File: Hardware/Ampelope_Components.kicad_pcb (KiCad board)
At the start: 4 copper layers, 60.5 x 81.6 mm, 101 parts, among them J1 Conn_01x12_Male, J18 SWD_Header, J19 USB_B_Micro, J2 Conn_01x12_Male, J3 Conn_01x12_Male, J4 Conn_01x12_Male, J5 Eurorack_16_pin_power, Q1 MMBT3906, Q2 MMBT3906, Q3 MMBT3906, Q4 MMBT3906, Q5 MMBT3906, U1 STM32G431RB, U2 AS3364, U3 LM1117-3.3, U4 TL074, U5 TL074, U6 TL074, Y1 8MHz 20pF

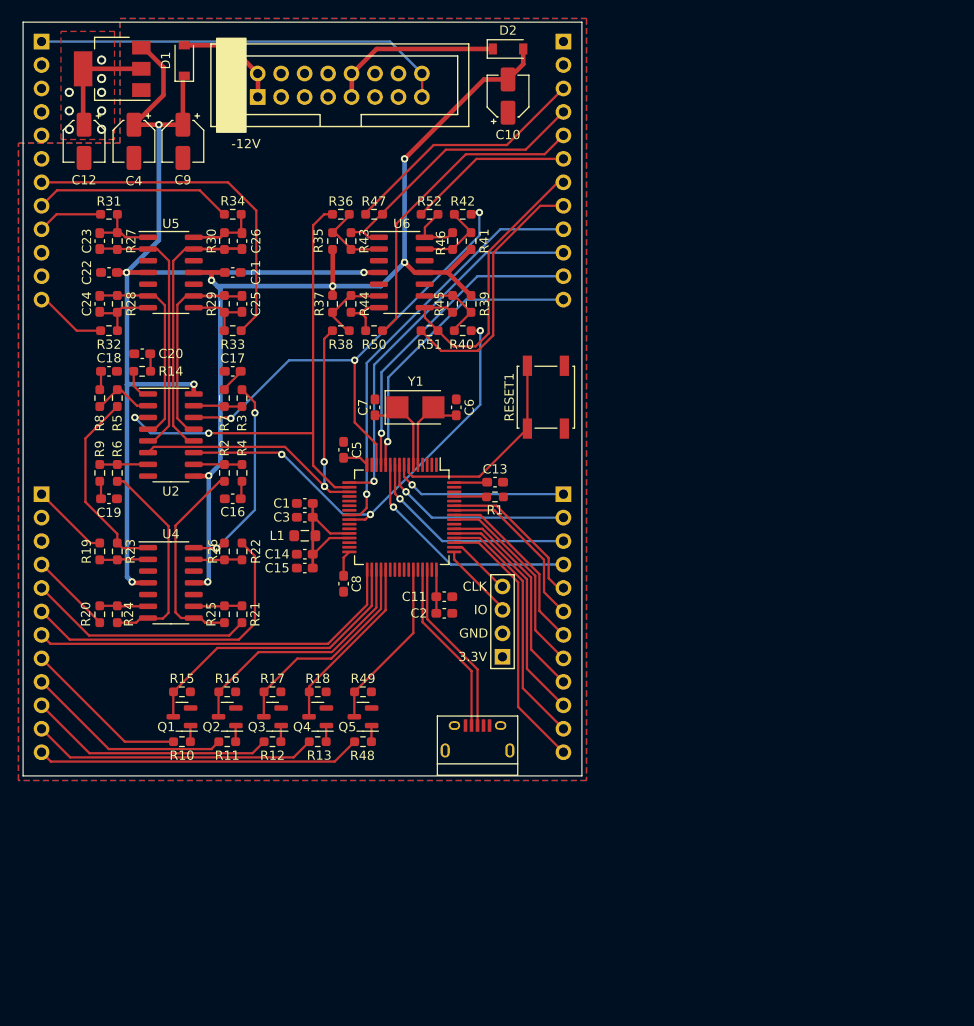
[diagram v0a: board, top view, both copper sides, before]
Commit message: Updates to component PCB to reflect VCA schematic changes
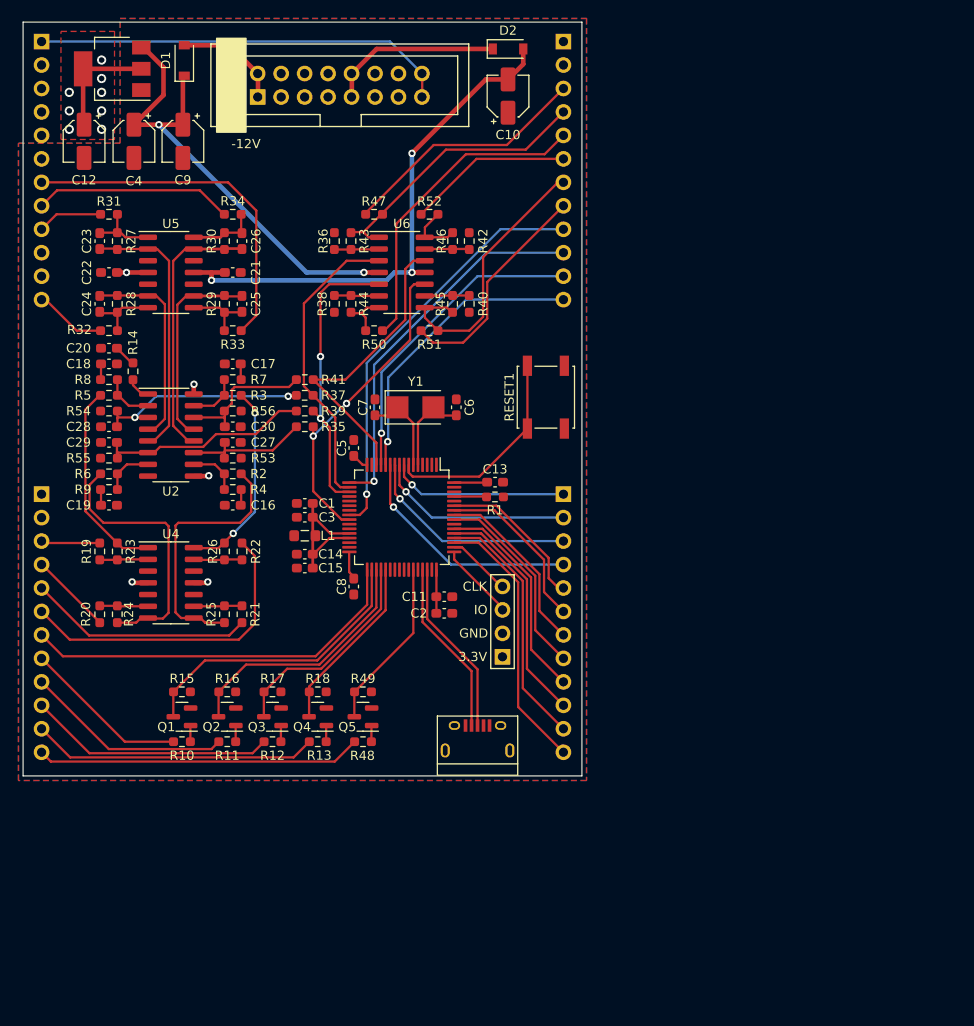
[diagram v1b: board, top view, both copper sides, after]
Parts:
- added C27: 2.2nF, Capacitor_SMD:C_0603_1608Metric_Pad1.08x0.95mm_HandSolder, F.Cu at (82.7, 70.9)
- added C28: 2.2nF, Capacitor_SMD:C_0603_1608Metric_Pad1.08x0.95mm_HandSolder, F.Cu at (69.3, 69.2)
- added C29: 2.2nF, Capacitor_SMD:C_0603_1608Metric_Pad1.08x0.95mm_HandSolder, F.Cu at (69.3, 70.9)
- added C30: 2.2nF, Capacitor_SMD:C_0603_1608Metric_Pad1.08x0.95mm_HandSolder, F.Cu at (82.7, 69.2)
- added R53: 10k, Resistor_SMD:R_0603_1608Metric_Pad0.98x0.95mm_HandSolder, F.Cu at (82.7, 72.6)
- added R54: 10k, Resistor_SMD:R_0603_1608Metric_Pad0.98x0.95mm_HandSolder, F.Cu at (69.3, 67.5)
- added R55: 10k, Resistor_SMD:R_0603_1608Metric_Pad0.98x0.95mm_HandSolder, F.Cu at (69.3, 72.6)
- added R56: 10k, Resistor_SMD:R_0603_1608Metric_Pad0.98x0.95mm_HandSolder, F.Cu at (82.7, 67.5)
- R35, R37, R39, R41: value 75k -> 6k8
- R36, R38, R40, R42: value 20k -> 3k3
- R43, R44, R45, R46: value 47k -> 4k7
- moved R41 23.4 mm to (90.5, 64.1), turned to 180 degrees
- moved R39 21.4 mm to (90.5, 67.5), turned to 180 degrees
- moved R35 20.3 mm to (90.5, 69.2), turned to 180 degrees
- moved R37 10.3 mm to (90.5, 65.8), turned to 180 degrees
- moved C20 3.65 mm to (69.3, 60.7)
- moved R36 2.98 mm to (93.7, 49.1), turned to 90 degrees
- moved R38 2.98 mm to (93.7, 55.9), turned to -90 degrees
- moved R40 2.98 mm to (108.3, 55.9), turned to -90 degrees
- moved R42 2.98 mm to (108.3, 49.1), turned to 90 degrees
- moved R8 2.24 mm to (69.3, 64.1), turned to 0 degrees
- moved R7 2.19 mm to (82.7, 64.1), turned to 180 degrees
- moved R4 2.06 mm to (82.7, 76.0), turned to 180 degrees
- moved R9 2.06 mm to (69.3, 76.0), turned to 0 degrees
- moved C8 1.14 mm to (95.8, 86.5)
- moved C5 1.12 mm to (95.8, 71.5)
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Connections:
- J19 pad 1: /USB_VBUS -> unconnected-(J19-Pad1)
- J2 pad 1: /Audio1_In -> unconnected-(J2-Pad1)
- J2 pad 3: unconnected-(J2-Pad3) -> /Audio1_In
- R35 pad 1: Net-(R35-Pad1) -> /Env3_DAC
- R35 pad 2: VEE -> /Env3_Scaled
- R36 pad 1: Net-(R35-Pad1) -> Net-(R36-Pad1)
- R36 pad 2: /Env1_DAC -> GND
- R37 pad 1: Net-(R37-Pad1) -> /Env1_DAC
- R37 pad 2: VEE -> /Env1_Scaled
- R38 pad 1: Net-(R37-Pad1) -> Net-(R38-Pad1)
- R38 pad 2: /Env2_DAC -> GND
- R39 pad 1: Net-(R39-Pad1) -> /Env2_DAC
- R39 pad 2: VEE -> /Env2_Scaled
- R40 pad 1: Net-(R39-Pad1) -> Net-(R40-Pad1)
- R40 pad 2: /Env3_DAC -> GND
- R41 pad 1: Net-(R41-Pad1) -> /Env4_DAC
- R41 pad 2: VEE -> /Env4_Scaled
- R42 pad 1: Net-(R41-Pad1) -> Net-(R42-Pad1)
- R42 pad 2: /Env4_DAC -> GND
- R43 pad 2: Net-(R35-Pad1) -> Net-(R36-Pad1)
- R44 pad 2: Net-(R37-Pad1) -> Net-(R38-Pad1)
- R45 pad 2: Net-(R39-Pad1) -> Net-(R40-Pad1)
- R46 pad 2: Net-(R41-Pad1) -> Net-(R42-Pad1)
- U2 pad 11: /Env3_DAC -> /Env3_Scaled
- U2 pad 14: /Env4_DAC -> /Env4_Scaled
- U2 pad 3: /Env1_DAC -> /Env1_Scaled
- U2 pad 6: /Env2_DAC -> /Env2_Scaled
- U6 pad 10: GND -> /Env3_DAC
- U6 pad 12: GND -> /Env4_DAC
- U6 pad 13: Net-(R41-Pad1) -> Net-(R42-Pad1)
- U6 pad 2: Net-(R35-Pad1) -> Net-(R36-Pad1)
- U6 pad 3: GND -> /Env1_DAC
- U6 pad 5: GND -> /Env2_DAC
- U6 pad 6: Net-(R37-Pad1) -> Net-(R38-Pad1)
- U6 pad 9: Net-(R39-Pad1) -> Net-(R40-Pad1)
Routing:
- net /Env1_Scaled: track 0.00 -> 23.5 mm, vias 0 -> 2
- net /Env1_DAC: track 55.0 -> 32.5 mm, vias 2 -> 0
- net /Env2_Scaled: track 0.00 -> 22.3 mm
- net /Env4_DAC: track 54.9 -> 32.7 mm, vias 3 -> 0
- net /Env3_DAC: track 50.2 -> 34.3 mm, vias 3 -> 2
- net /Env4_Scaled: track 0.00 -> 15.1 mm
- net VEE: track 110.0 -> 95.9 mm, vias 6 -> 5
- net /Env3_Scaled: track 0.00 -> 13.9 mm
- net /Env2_DAC: track 41.3 -> 31.5 mm
- net Net-(R39-Pad1): track 8.14 -> 0.00 mm
- net Net-(R41-Pad1): track 8.08 -> 0.00 mm
- net Net-(R37-Pad1): track 8.05 -> 0.00 mm
- net Net-(R35-Pad1): track 8.04 -> 0.00 mm
- net /Audio3_In_Buff: track 21.7 -> 27.8 mm
- net /Audio2_In_Buff: track 22.1 -> 28.2 mm
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
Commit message: Added test points to component PCB; Added 3D mockups
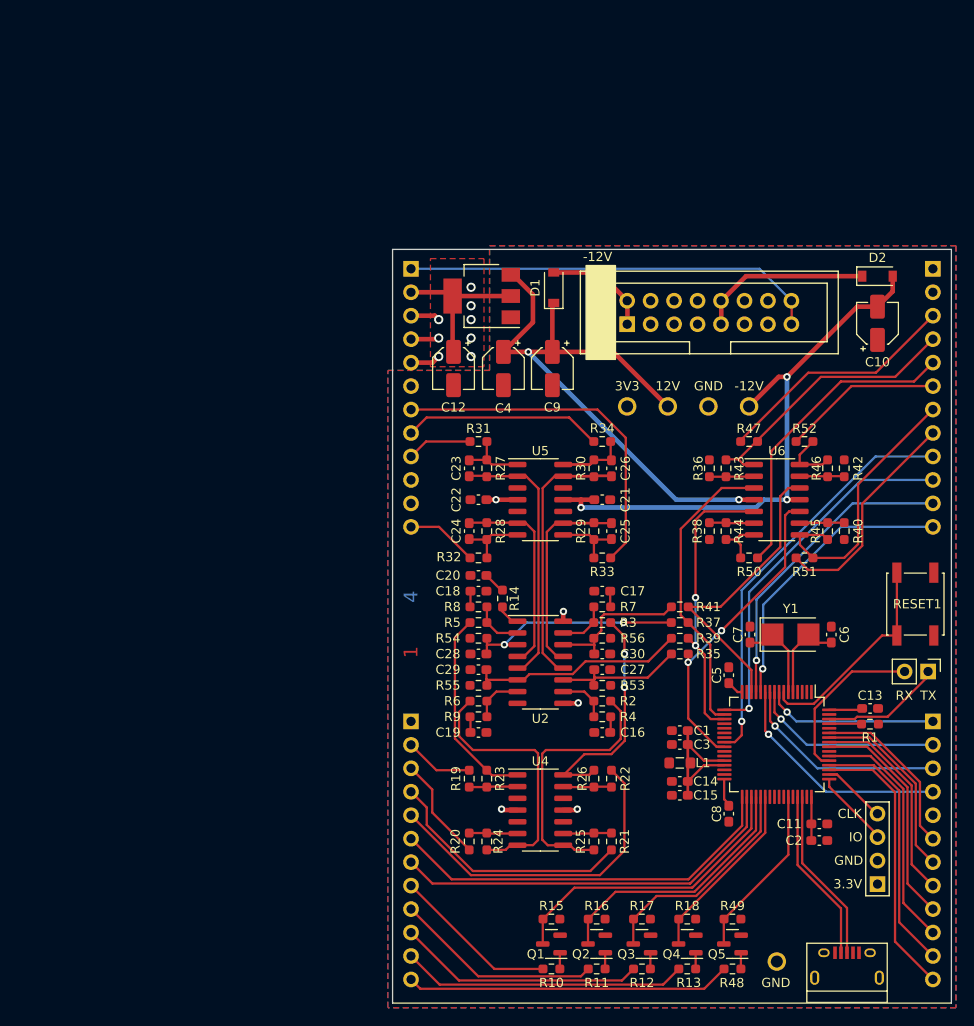
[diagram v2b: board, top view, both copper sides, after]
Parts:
- added FID1: 4_Layer_Marker, Custom_Footprints:4_Layer_Markers, F.Cu at (102.0, 90.6)
- added J6: Conn_01x02_Male, Connector_PinHeader_2.54mm:PinHeader_1x02_P2.54mm_Vertical, F.Cu at (158.0, 95.7)
- added TP1: TestPoint, Custom_Footprints:1.3mm_Test_Point, F.Cu at (134.2, 67.0)
- added TP2: TestPoint, Custom_Footprints:1.3mm_Test_Point, F.Cu at (125.4, 67.0)
- added TP3: TestPoint, Custom_Footprints:1.3mm_Test_Point, F.Cu at (129.8, 67.0)
- added TP4: TestPoint, Custom_Footprints:1.3mm_Test_Point, F.Cu at (138.6, 67.0)
- added TP5: TestPoint, Custom_Footprints:1.3mm_Test_Point, F.Cu at (141.6, 127.1)
- moved C5 47.5 mm to (136.4, 96.1)
- moved C8 47.5 mm to (136.4, 111.1)
- moved R36 47.5 mm to (134.3, 73.7)
- moved R37 47.5 mm to (131.1, 90.4)
- moved R38 47.5 mm to (134.3, 80.5)
- moved R40 47.5 mm to (148.9, 80.5)
- moved R42 47.5 mm to (148.9, 73.7)
- moved C11 47.5 mm to (146.2, 112.2)
- moved C6 47.5 mm to (147.5, 91.7)
- moved C7 47.5 mm to (138.7, 91.7)
- moved R1 47.5 mm to (151.7, 101.4)
- moved R41 47.5 mm to (131.1, 88.7)
- moved R50 47.5 mm to (138.6, 83.4)
- moved R51 47.5 mm to (144.6, 83.4)
- moved Y1 47.5 mm to (143.1, 91.7)
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- renumbered J18 to J7, J19 to J8
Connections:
- J1 pad 10: unconnected-(J1-Pad10) -> GND
- J1 pad 11: unconnected-(J1-Pad11) -> GND
- J1 pad 2: unconnected-(J1-Pad2) -> +3V3
- J1 pad 3: unconnected-(J1-Pad3) -> +3V3
- J1 pad 4: unconnected-(J1-Pad4) -> +3V3
- J1 pad 5: unconnected-(J1-Pad5) -> +3V3
- J1 pad 6: unconnected-(J1-Pad6) -> GND
- J2 pad 1: unconnected-(J2-Pad1) -> GND
- J2 pad 2: unconnected-(J2-Pad2) -> /Audio1_In
- J2 pad 3: /Audio1_In -> /Audio2_In
- J2 pad 4: /Audio2_In -> /Audio3_In
- J2 pad 5: /Audio3_In -> /Audio4_In
- J2 pad 6: /Audio4_In -> /LFO_Speed
- J2 pad 7: /LFO_Speed -> /Env4_Short
- J3 pad 1: unconnected-(J3-Pad1) -> GND
- J3 pad 2: unconnected-(J3-Pad2) -> GND
- J4 pad 10: /Env4_Short -> /Env3_LFO
- J4 pad 11: /Env3_LFO -> /Env3_Short
- J4 pad 12: /Env3_Short -> /Env4_LFO
- J4 pad 5: /Env2_LFO -> GND
- J4 pad 6: /Env2_Short -> /Env1_LFO
- J4 pad 7: /Env1_LFO -> /Env1_Short
- J4 pad 8: /Env1_Short -> /Env2_LFO
- J4 pad 9: /Env4_LFO -> /Env2_Short
- U1 pad 34: /Gate1_Inv -> /Env4_Short
- U1 pad 35: /Gate2_Inv -> /Gate1_Inv
- U1 pad 36: /Gate3_Inv -> /Gate2_Inv
- U1 pad 37: /Gate4_Inv -> /Gate3_Inv
- U1 pad 38: unconnected-(U1-Pad38) -> /Gate4_Inv
- U1 pad 51: /Env3_Short -> /Env4_LFO
- U1 pad 52: /Env3_LFO -> /Env3_Short
- U1 pad 53: /Env4_Short -> /UART3_RX
- U1 pad 54: /Env4_LFO -> /Env3_LFO
- U1 pad 56: /Env1_Short -> /Env2_Short
- U1 pad 57: /Env1_LFO -> /Env2_LFO
- U1 pad 58: /Env2_Short -> /Env1_Short
- U1 pad 59: /Env2_LFO -> /Env1_LFO
- U1 pad 62: unconnected-(U1-Pad62) -> /UART3_TX
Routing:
- net /UART3_RX: track 0.00 -> 18.2 mm
- net /Env4_Short: track 25.2 -> 43.1 mm
- net VCC: track 114.5 -> 130.0 mm
- net +3V3: track 24.9 -> 38.5 mm
- net /UART3_TX: track 0.00 -> 13.1 mm
- net /Env4_LFO: track 23.3 -> 30.1 mm
- net /Env2_LFO: track 16.3 -> 22.7 mm
- net /Env2_Short: track 18.4 -> 24.6 mm
- net VEE: track 95.9 -> 101.5 mm
- net /Audio4_In_Buff: track 21.5 -> 25.2 mm
- net /Audio3_In: track 24.4 -> 27.3 mm
- net /Audio2_In: track 9.12 -> 11.4 mm
- net /Audio4_In: track 34.4 -> 36.2 mm
- net /Audio1_In: track 6.09 -> 7.44 mm
- net /Env3_Short: track 29.1 -> 28.1 mm
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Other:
- board text added: "-12V"
- board text added: "12V"
- board text added: "3V3"
- board text added: "GND"
- board text added: "RX"
- board text added: "TX"

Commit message: Fixed DRC errors on control and component boards
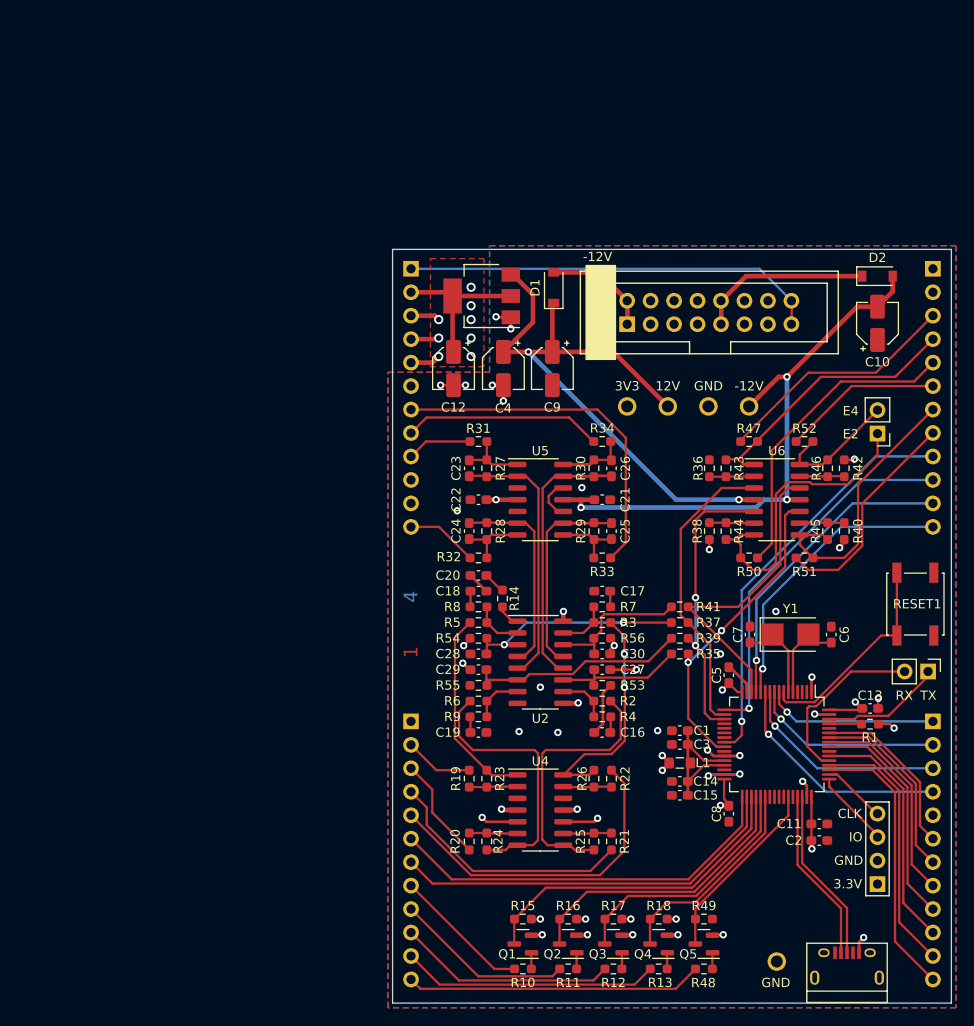
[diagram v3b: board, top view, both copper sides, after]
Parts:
- added J9: Conn_01x02_Male, Connector_PinHeader_2.54mm:PinHeader_1x02_P2.54mm_Vertical, F.Cu at (152.5, 69.9)
- moved Q1 3.09 mm to (114.1, 125.2)
- moved Q3 3.09 mm to (123.9, 125.2)
- moved Q4 3.09 mm to (128.8, 125.2)
- moved Q5 3.09 mm to (133.7, 125.2)
- moved R10 3.09 mm to (114.1, 127.9)
- moved R12 3.09 mm to (123.9, 127.9)
- moved R13 3.09 mm to (128.8, 127.9)
- moved R15 3.09 mm to (114.1, 122.5)
- moved R17 3.09 mm to (123.9, 122.5)
- moved R18 3.09 mm to (128.8, 122.5)
- moved R48 3.09 mm to (133.7, 127.9)
- moved R49 3.09 mm to (133.7, 122.5)
- moved Q2 3.09 mm to (119.0, 125.2)
- moved R11 3.09 mm to (119.0, 127.9)
- moved R16 3.09 mm to (119.0, 122.5)
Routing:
- net GND: track 0.75 -> 62.1 mm, vias 0 -> 36
- net /Env2_Out: track 5.33 -> 32.7 mm
- net +3V3: track 38.5 -> 52.0 mm, vias 8 -> 20
- net /Env4_Out: track 6.37 -> 14.0 mm
- net /Gate4_Inv: track 19.8 -> 22.9 mm
- net /Gate3_Inv: track 24.1 -> 27.2 mm
- net /Gate2_Inv: track 28.4 -> 31.5 mm
- net /Gate2_In: track 22.5 -> 19.4 mm
- net /Gate4_In: track 31.0 -> 27.9 mm
- net /Gate3_In: track 26.8 -> 23.7 mm
- net /Gate1_Inv: track 32.7 -> 35.8 mm
- net /Gate1_In: track 18.0 -> 14.9 mm
- net /Clock_In: track 35.2 -> 32.1 mm
- net /Clock_Inv: track 18.8 -> 20.1 mm
- net /UART3_RX: track 18.2 -> 19.4 mm
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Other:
- board text added: "E2"
- board text added: "E4"
